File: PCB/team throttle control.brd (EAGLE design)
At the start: 75.9 x 59.7 mm, 15 parts, among them IC1 ICL7663CPA, IC4 7805T

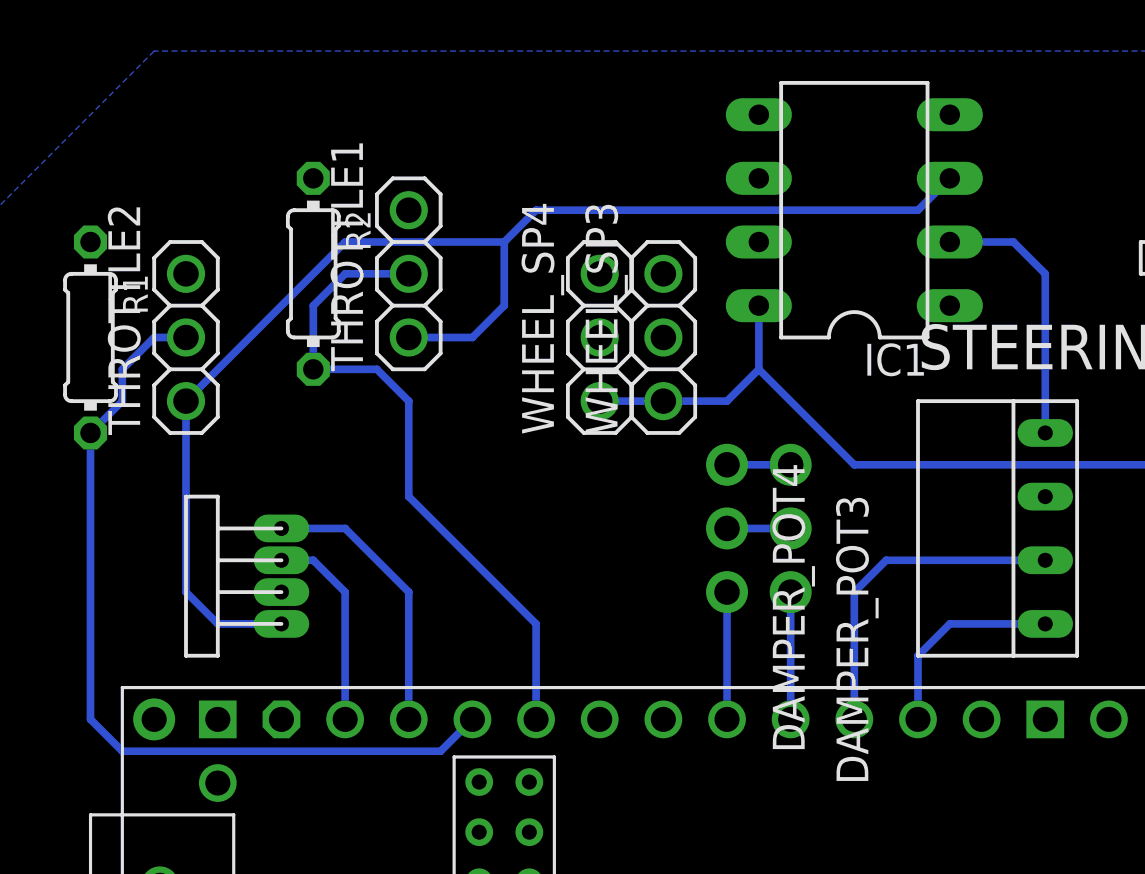
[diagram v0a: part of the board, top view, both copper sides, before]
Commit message: Stress board for Wheat bridge and edits
Created the Wheat bridge board with the different stress gauges in the F-E library. There were some minor edits that the other boards needed as well.
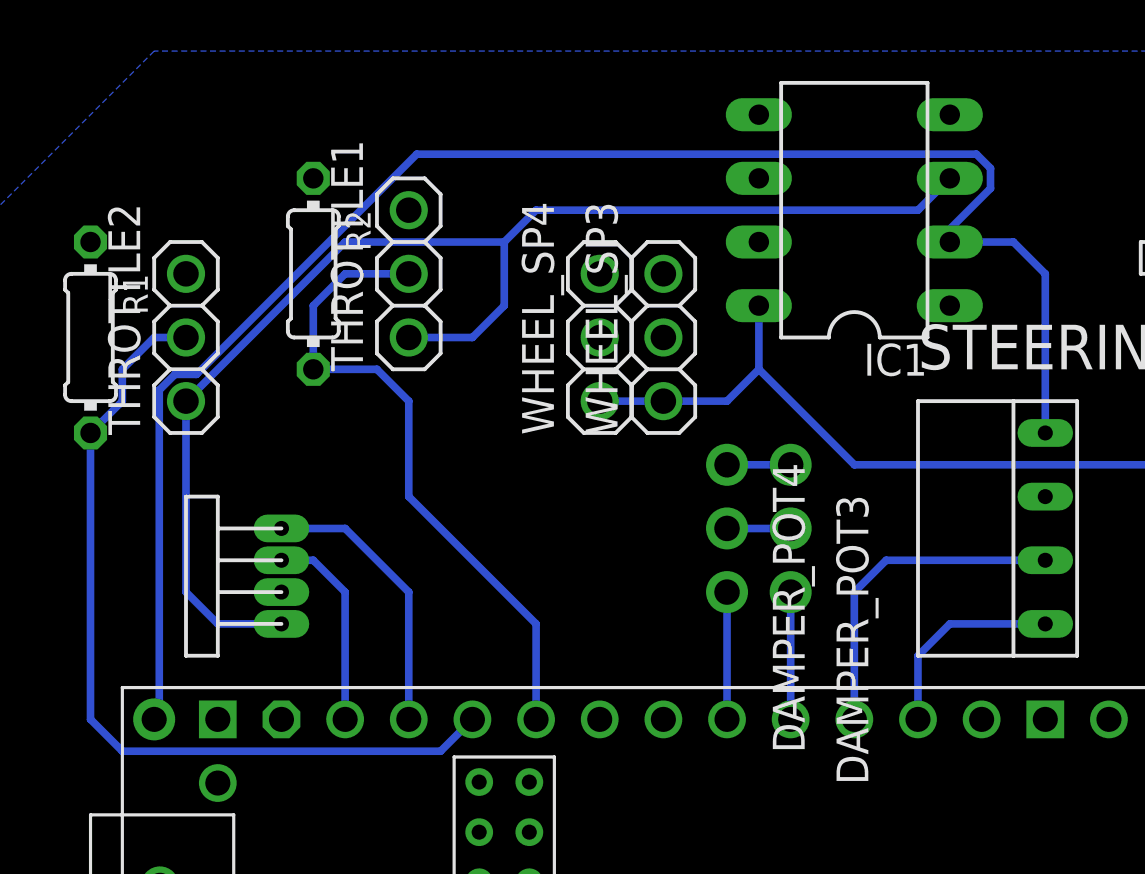
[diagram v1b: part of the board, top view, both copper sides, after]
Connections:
- net 5V: now also U$3.VIN
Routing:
- net 5V: track 10.7 -> 64.8 mm
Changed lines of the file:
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@@
 <wire x1="67.31" y1="69.85" x2="68.58" y2="68.58" width="0.3048" layer="16"/>
 <wire x1="68.58" y1="68.58" x2="68.58" y2="62.23" width="0.3048" layer="16"/>
+<contactref element="U$3" pad="VIN"/>
+<wire x1="33.2232" y1="63.9418875" x2="33.8481125" y2="64.5668" width="0.3048" layer="16"/>
+<wire x1="33.8481125" y1="64.5668" x2="34.71021875" y2="64.5668" width="0.3048" layer="16"/>
+<wire x1="65.8302" y1="73.3552" x2="66.3956" y2="72.7898" width="0.3048" layer="16"/>
+<wire x1="66.3956" y1="72.7898" x2="66.3956" y2="71.9902" width="0.3048" layer="16"/>
+<wire x1="33.02" y1="50.8" x2="33.2232" y2="51.0032" width="0.3048" layer="16"/>
+<wire x1="33.2232" y1="51.0032" x2="33.2232" y2="63.9418875" width="0.3048" layer="16"/>
+<wire x1="66.3956" y1="71.9902" x2="64.77" y2="70.3646" width="0.3048" layer="16"/>
+<wire x1="64.77" y1="70.3646" x2="64.77" y2="69.85" width="0.3048" layer="16"/>
+<wire x1="34.71021875" y1="64.5668" x2="43.49861875" y2="73.3552" width="0.3048" layer="16"/>
+<wire x1="43.49861875" y1="73.3552" x2="65.8302" y2="73.3552" width="0.3048" layer="16"/>
 </signal>
 <signal name="T2_DP_2">

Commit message: small update on throttle
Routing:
- net WH_SP3_D: track 0.00 -> 19.1 mm
- net WH_SP4_D: track 0.00 -> 16.5 mm
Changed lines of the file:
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@@
 <contactref element="WHEEL_SP3" pad="2"/>
 <contactref element="U$3" pad="18-A4/SDA0"/>
-<wire x1="53.34" y1="50.8" x2="53.34" y2="66.04" width="0" layer="19" extent="1-1"/>
+<wire x1="50.3581125" y1="64.5668" x2="49.7332" y2="63.9418875" width="0.3048" layer="16"/>
+<wire x1="49.7332" y1="63.9418875" x2="49.7332" y2="63.0581125" width="0.3048" layer="16"/>
+<wire x1="53.34" y1="59.4513125" x2="53.34" y2="50.8" width="0.3048" layer="16"/>
+<wire x1="49.7332" y1="63.0581125" x2="53.34" y2="59.4513125" width="0.3048" layer="16"/>
+<wire x1="53.34" y1="66.04" x2="51.8668" y2="64.5668" width="0.3048" layer="16"/>
+<wire x1="51.8668" y1="64.5668" x2="50.3581125" y2="64.5668" width="0.3048" layer="16"/>
 </signal>
 <signal name="WH_SP4_D">
 <contactref element="WHEEL_SP4" pad="2"/>
 <contactref element="U$3" pad="19-A5/SCL0"/>
-<wire x1="50.8" y1="50.8" x2="50.8" y2="66.04" width="0" layer="19" extent="1-1"/>
+<wire x1="50.8" y1="61.34473125" x2="50.8" y2="50.8" width="0.3048" layer="16"/>
+<wire x1="49.276" y1="64.13126875" x2="49.276" y2="62.86873125" width="0.3048" layer="16"/>
+<wire x1="49.276" y1="62.86873125" x2="50.8" y2="61.34473125" width="0.3048" layer="16"/>
+<wire x1="50.8" y1="66.04" x2="50.8" y2="65.65526875" width="0.3048" layer="16"/>
+<wire x1="50.8" y1="65.65526875" x2="49.276" y2="64.13126875" width="0.3048" layer="16"/>
 </signal>
 <signal name="ACC_DATA_OUT_1">
